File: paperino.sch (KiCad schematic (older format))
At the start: 19 parts, among them P1 CONN_01X06, P2 CONN_01X06, Q1 PMOS, Q2 NMOS, U1 BMA250E, X1 XF2M-2615-1A, X2 XF2B-4545-1A

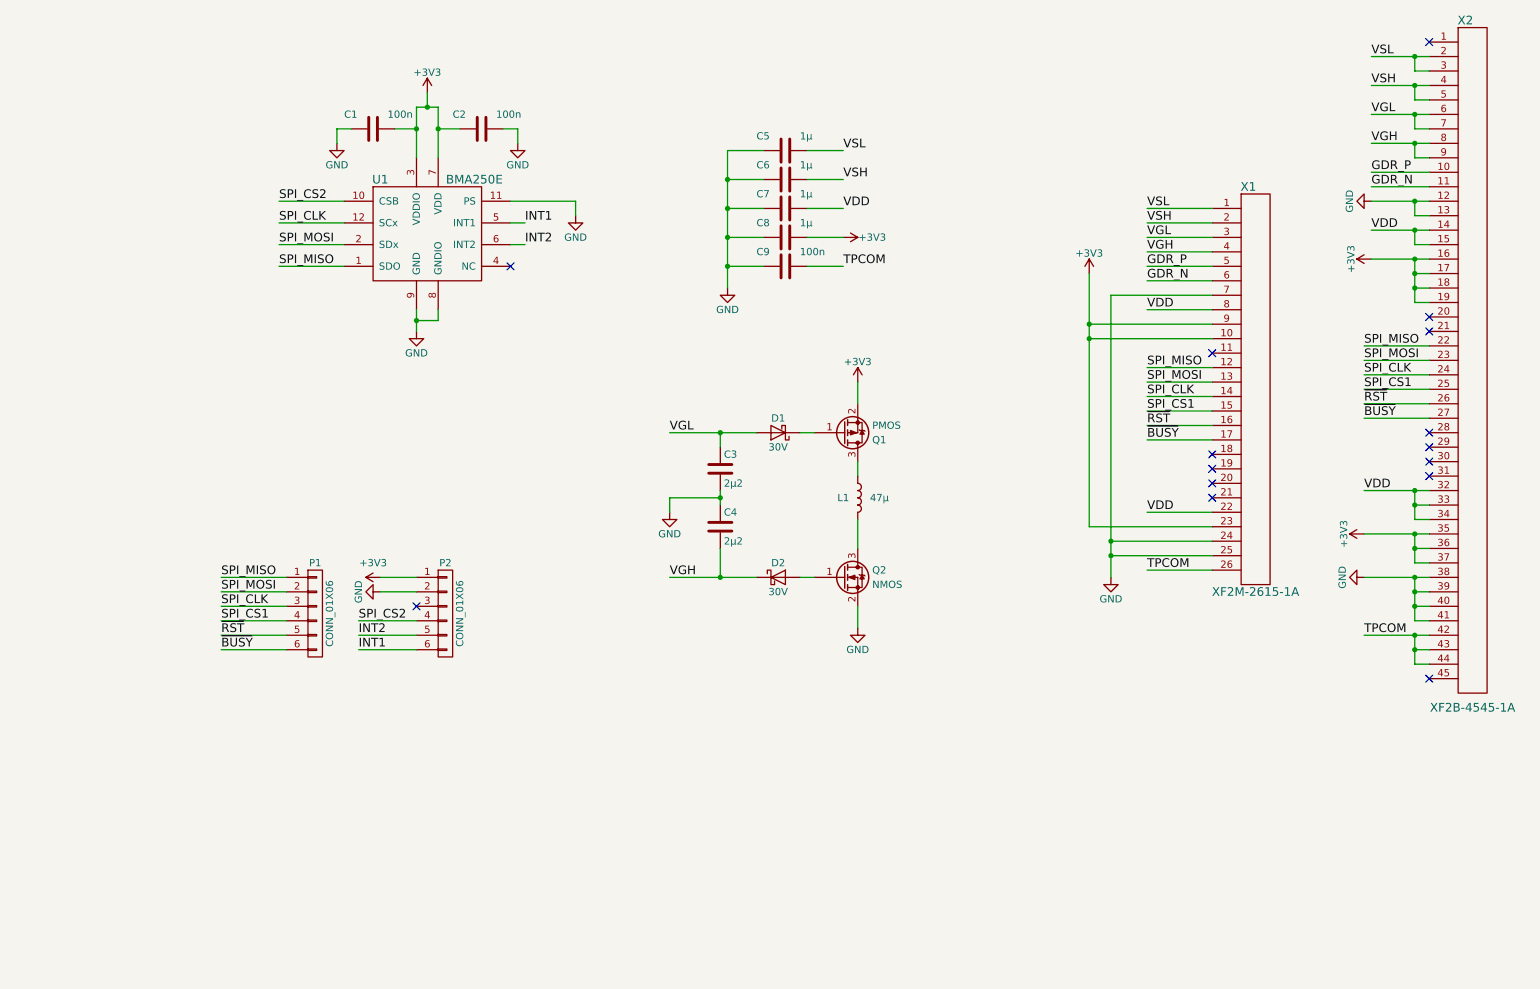
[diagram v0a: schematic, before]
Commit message: error in booster circuit corrected
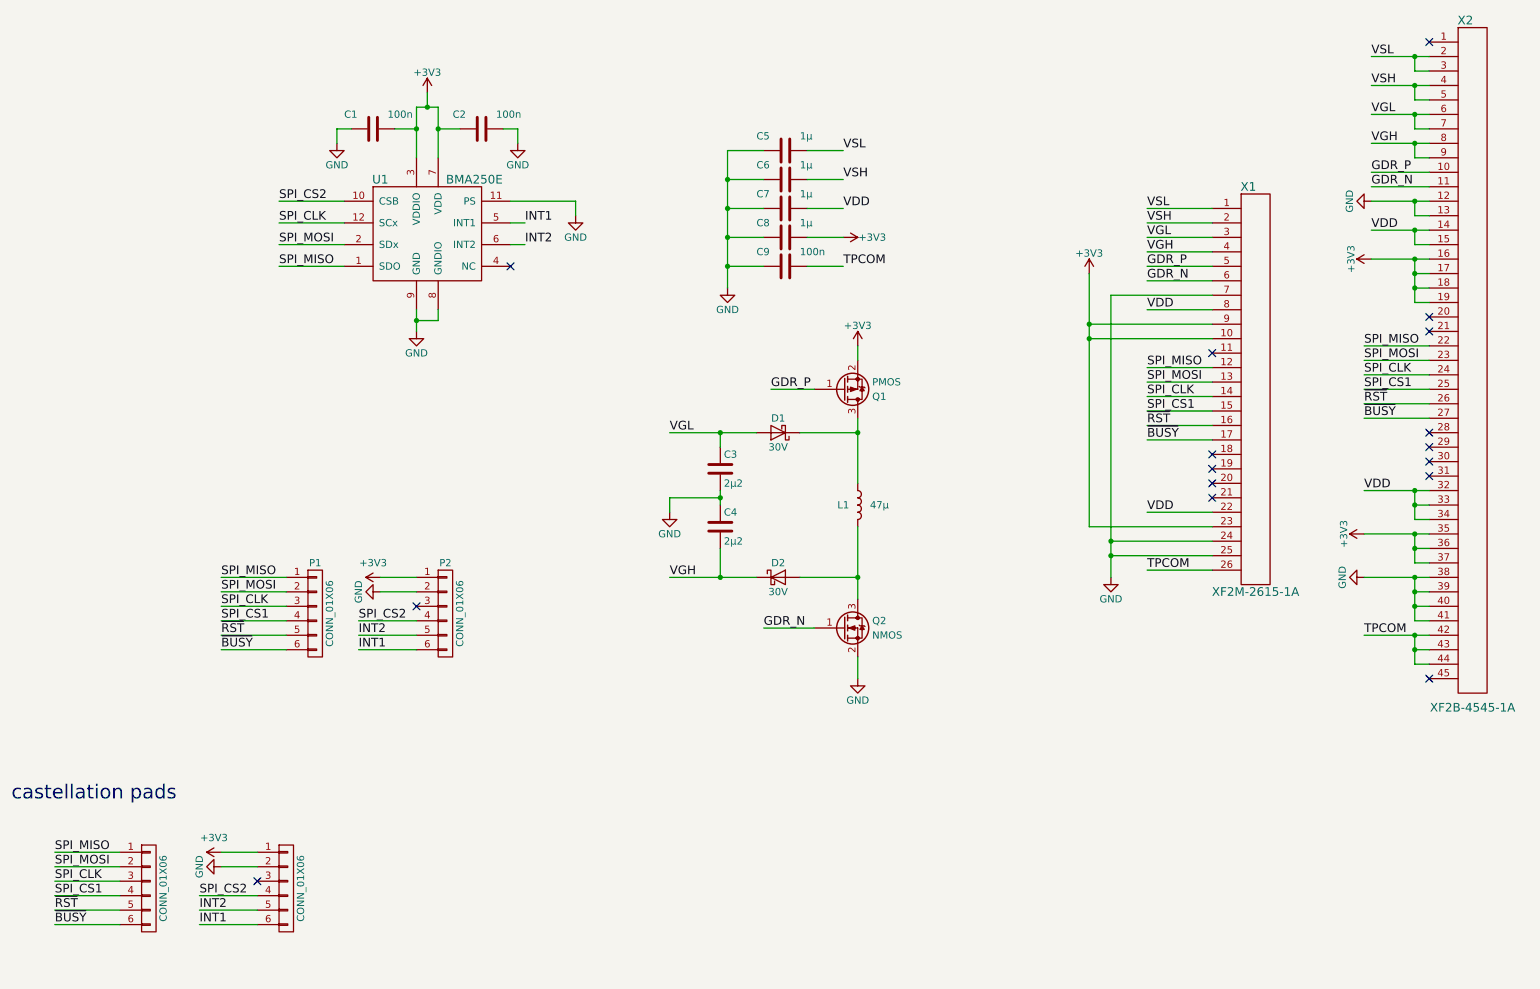
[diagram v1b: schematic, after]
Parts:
- added P3, P4: CONN_01X06, Paperino:1x6_header, symbol CONN_01X06
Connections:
- net +3V3: now also P4.1 (P1)
- net GDR_N: now also Q2.1 (G)
- net GDR_P: now also Q1.1 (G)
- net GND: now also P4.2 (P2)
- net INT1: now also P4.6 (P6)
- net INT2: now also P4.5 (P5)
- net SPI_CLK: now also P3.3 (P3)
- net SPI_CS1: now also P3.4 (P4)
- net SPI_CS2: now also P4.4 (P4)
- net SPI_MISO: now also P3.1 (P1)
- net SPI_MOSI: now also P3.2 (P2)
- net ~BUSY: now also P3.6 (P6)
- net ~RST: now also P3.5 (P5)
- net at L1.1, Q1.3 (D): now also D1.1 (K)
- net at L1.2, Q2.3 (D): now also D2.2 (A)
- no-connect marks 15 -> 16
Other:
- note added: "castellation pads"
- moved on the sheet: L1, Q1, Q2
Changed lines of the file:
@@
 L L L1
 U 1 1 589DD1F6
-P 6500 4400
-F 0 "L1" H 6400 4400 50  0000 C CNN
-F 1 "47µ" H 6650 4400 50  0000 C CNN
-F 2 "Paperino:NR4018T470M" H 6500 4400 50  0001 C CNN
-F 3 "" H 6500 4400 50  0000 C CNN
-	1    6500 4400
+P 6500 4450
+F 0 "L1" H 6400 4450 50  0000 C CNN
+F 1 "47µ" H 6650 4450 50  0000 C CNN
+F 2 "Paperino:NR4018T470M" H 6500 4450 50  0001 C CNN
+F 3 "" H 6500 4450 50  0000 C CNN
+	1    6500 4450
 	1    0    0    -1
 $EndComp
@@
 L Q_NMOS_GSD Q2
 U 1 1 589DD9DD
-P 6400 4950
-F 0 "Q2" H 6600 5000 50  0000 L CNN
-F 1 "NMOS" H 6600 4900 50  0000 L CNN
-F 2 "TO_SOT_Packages_SMD:SOT-323_SC-70" H 6600 5050 50  0001 C CNN
-F 3 "" H 6400 4950 50  0000 C CNN
-	1    6400 4950
-	1    0    0    -1
-$EndComp
-Wire Wire Line
-	6500 4750 6500 4550
+P 6400 5300
+F 0 "Q2" H 6600 5350 50  0000 L CNN
+F 1 "NMOS" H 6600 5250 50  0000 L CNN
+F 2 "TO_SOT_Packages_SMD:SOT-323_SC-70" H 6600 5400 50  0001 C CNN
+F 3 "" H 6400 5300 50  0000 C CNN
+	1    6400 5300
+	1    0    0    -1
+$EndComp
+Wire Wire Line
+	6500 4600 6500 5100
 $Comp
 L GND #PWR06
 U 1 1 589DDF8E
-P 6500 5300
-F 0 "#PWR06" H 6500 5050 50  0001 C CNN
-F 1 "GND" H 6500 5150 50  0000 C CNN
-F 2 "" H 6500 5300 50  0000 C CNN
-F 3 "" H 6500 5300 50  0000 C CNN
-	1    6500 5300
+P 6500 5650
+F 0 "#PWR06" H 6500 5400 50  0001 C CNN
+F 1 "GND" H 6500 5500 50  0000 C CNN
+F 2 "" H 6500 5650 50  0000 C CNN
+F 3 "" H 6500 5650 50  0000 C CNN
+	1    6500 5650
 	1    0    0    -1
 $EndComp
@@
 L +3V3 #PWR07
 U 1 1 589DE04D
-P 6500 3600
-F 0 "#PWR07" H 6500 3450 50  0001 C CNN
-F 1 "+3V3" H 6500 3740 50  0000 C CNN
-F 2 "" H 6500 3600 50  0000 C CNN
-F 3 "" H 6500 3600 50  0000 C CNN
-	1    6500 3600
+P 6500 3350
+F 0 "#PWR07" H 6500 3200 50  0001 C CNN
+F 1 "+3V3" H 6500 3490 50  0000 C CNN
+F 2 "" H 6500 3350 50  0000 C CNN
+F 3 "" H 6500 3350 50  0000 C CNN
+	1    6500 3350
 	1    0    0    -1
 $EndComp
@@
 L Q_PMOS_GSD Q1
 U 1 1 589DE096
-P 6400 3950
-F 0 "Q1" H 6600 4000 50  0000 L CNN
-F 1 "PMOS" H 6600 3900 50  0000 L CNN
-F 2 "Paperino:SC-59" H 6600 4050 50  0001 C CNN
-F 3 "" H 6400 3950 50  0000 C CNN
-	1    6400 3950
+P 6400 3650
+F 0 "Q1" H 6600 3700 50  0000 L CNN
+F 1 "PMOS" H 6600 3600 50  0000 L CNN
+F 2 "Paperino:SC-59" H 6600 3750 50  0001 C CNN
+F 3 "" H 6400 3650 50  0000 C CNN
+	1    6400 3650
 	1    0    0    1
 $EndComp
 Wire Wire Line
-	6500 4250 6500 4150
-Wire Wire Line
-	6500 5300 6500 5150
-Wire Wire Line
-	6500 3600 6500 3750
+	6500 5650 6500 5500
+Wire Wire Line
+	6500 3350 6500 3450
 $Comp
 L BMA250E U1
@@
 $EndComp
 Wire Wire Line
-	6100 3950 6200 3950
-Wire Wire Line
-	6100 4950 6200 4950
+	6100 3950 6500 3950
+Wire Wire Line
+	6500 4950 6100 4950
 $Comp
 L +3V3 #PWR010
@@
 Wire Wire Line
 	2100 5450 2550 5450
+$Comp
+L CONN_01X06 P3
+U 1 1 58A6EC07
+P 1600 7100
+F 0 "P3" H 1600 7450 50  0001 C CNN
+F 1 "CONN_01X06" V 1700 7100 50  0000 C CNN
+F 2 "Paperino:1x6_header" H 1600 7100 50  0001 C CNN
+F 3 "" H 1600 7100 50  0000 C CNN
+	1    1600 7100
+	1    0    0    -1
+$EndComp
+Text Label 950  6950 0    60   ~ 0
+SPI_MOSI
+Text Label 950  6850 0    60   ~ 0
+SPI_MISO
+Text Label 950  7050 0    60   ~ 0
+SPI_CLK
+Text Label 950  7150 0    60   ~ 0
+SPI_CS1
+Text Label 950  7250 0    60   ~ 0
+~RST
+Text Label 950  7350 0    60   ~ 0
+~BUSY
+Wire Wire Line
+	950  6850 1400 6850
+Wire Wire Line
+	950  6950 1400 6950
+Wire Wire Line
+	950  7050 1400 7050
+Wire Wire Line
+	950  7150 1400 7150
+Wire Wire Line
+	1400 7250 950  7250
+Wire Wire Line
+	950  7350 1400 7350
+$Comp
+L CONN_01X06 P4
+U 1 1 58A6EEF6
+P 2550 7100
+F 0 "P4" H 2550 7450 50  0001 C CNN
+F 1 "CONN_01X06" V 2650 7100 50  0000 C CNN
+F 2 "Paperino:1x6_header" H 2550 7100 50  0001 C CNN
+F 3 "" H 2550 7100 50  0000 C CNN
+	1    2550 7100
+	1    0    0    -1
+$EndComp
+Text Label 1950 7150 0    60   ~ 0
+SPI_CS2
+Text Label 1950 7250 0    60   ~ 0
+INT2
+Text Label 1950 7350 0    60   ~ 0
+INT1
+$Comp
+L +3V3 #PWR019
+U 1 1 58A6EEFF
+P 2100 6850
+F 0 "#PWR019" H 2100 6700 50  0001 C CNN
+F 1 "+3V3" V 2200 6900 50  0000 C CNN
+F 2 "" H 2100 6850 50  0000 C CNN
+F 3 "" H 2100 6850 50  0000 C CNN
+	1    2100 6850
+	0    -1   -1   0
+$EndComp
+$Comp
+L GND #PWR020
+U 1 1 58A6EF05
+P 2100 6950
+F 0 "#PWR020" H 2100 6700 50  0001 C CNN
+F 1 "GND" H 2100 6800 50  0000 C CNN
+F 2 "" H 2100 6950 50  0000 C CNN
+F 3 "" H 2100 6950 50  0000 C CNN
+	1    2100 6950
+	0    1    1    0
+$EndComp
+Wire Wire Line
+	2100 6950 2350 6950
+Wire Wire Line
+	2350 6850 2100 6850
+NoConn ~ 2350 7050
+Wire Wire Line
+	1950 7150 2350 7150
+Wire Wire Line
+	2350 7250 1950 7250
+Wire Wire Line
+	1950 7350 2350 7350
+Text Notes 650  6500 0    98   ~ 0
+castellation pads
+Text Label 5850 5300 0    60   ~ 0
+GDR_N
+Text Label 5900 3650 0    60   ~ 0
+GDR_P
+Wire Wire Line
+	5900 3650 6200 3650
+Wire Wire Line
+	5850 5300 6200 5300
+Connection ~ 6500 4950
+Wire Wire Line
+	6500 3850 6500 4300
+Connection ~ 6500 3950
 $EndSCHEMATC

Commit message: fiducials added
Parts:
- added Fid1, Fid2: Fiducial, Paperino:Fiducial, symbol Fiducial
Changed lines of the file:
@@
 U 1 1 589DD9DD
 P 6400 5300
-F 0 "Q2" H 6600 5350 50  0000 L CNN
-F 1 "NMOS" H 6600 5250 50  0000 L CNN
+F 0 "Q2" H 6600 5300 50  0000 L CNN
+F 1 "NMOS" H 6600 5250 50  0001 L CNN
 F 2 "TO_SOT_Packages_SMD:SOT-323_SC-70" H 6600 5400 50  0001 C CNN
 F 3 "" H 6400 5300 50  0000 C CNN
@@
 U 1 1 589DE096
 P 6400 3650
-F 0 "Q1" H 6600 3700 50  0000 L CNN
-F 1 "PMOS" H 6600 3600 50  0000 L CNN
+F 0 "Q1" H 6600 3650 50  0000 L CNN
+F 1 "PMOS" H 6600 3600 50  0001 L CNN
 F 2 "Paperino:SC-59" H 6600 3750 50  0001 C CNN
 F 3 "" H 6400 3650 50  0000 C CNN
@@
 P 2750 5200
 F 0 "P1" H 2750 5550 50  0000 C CNN
-F 1 "CONN_01X06" V 2850 5200 50  0000 C CNN
+F 1 "CONN_01X06" V 2850 5200 50  0001 C CNN
 F 2 "Paperino:1x6_header" H 2750 5200 50  0001 C CNN
 F 3 "" H 2750 5200 50  0000 C CNN
@@
 P 3650 5200
 F 0 "P2" H 3650 5550 50  0000 C CNN
-F 1 "CONN_01X06" V 3750 5200 50  0000 C CNN
+F 1 "CONN_01X06" V 3750 5200 50  0001 C CNN
 F 2 "Paperino:1x6_header" H 3650 5200 50  0001 C CNN
 F 3 "" H 3650 5200 50  0000 C CNN
@@
 P 1600 7100
 F 0 "P3" H 1600 7450 50  0001 C CNN
-F 1 "CONN_01X06" V 1700 7100 50  0000 C CNN
+F 1 "CONN_01X06" V 1700 7100 50  0001 C CNN
 F 2 "Paperino:1x6_header" H 1600 7100 50  0001 C CNN
 F 3 "" H 1600 7100 50  0000 C CNN
@@
 P 2550 7100
 F 0 "P4" H 2550 7450 50  0001 C CNN
-F 1 "CONN_01X06" V 2650 7100 50  0000 C CNN
+F 1 "CONN_01X06" V 2650 7100 50  0001 C CNN
 F 2 "Paperino:1x6_header" H 2550 7100 50  0001 C CNN
 F 3 "" H 2550 7100 50  0000 C CNN
@@
 	6500 3850 6500 4300
 Connection ~ 6500 3950
+$Comp
+L Fiducial Fid1
+U 1 1 58B53A2F
+P 6300 7450
+F 0 "Fid1" H 6300 7250 60  0000 C CNN
+F 1 "Fiducial" H 6300 7700 60  0001 C CNN
+F 2 "Paperino:Fiducial" H 6300 7450 60  0001 C CNN
+F 3 "" H 6300 7450 60  0001 C CNN
+	1    6300 7450
+	1    0    0    -1
+$EndComp
+$Comp
+L Fiducial Fid2
+U 1 1 58B53F28
+P 6700 7450
+F 0 "Fid2" H 6700 7250 60  0000 C CNN
+F 1 "Fiducial" H 6700 7700 60  0001 C CNN
+F 2 "Paperino:Fiducial" H 6700 7450 60  0001 C CNN
+F 3 "" H 6700 7450 60  0001 C CNN
+	1    6700 7450
+	1    0    0    -1
+$EndComp
 $EndSCHEMATC

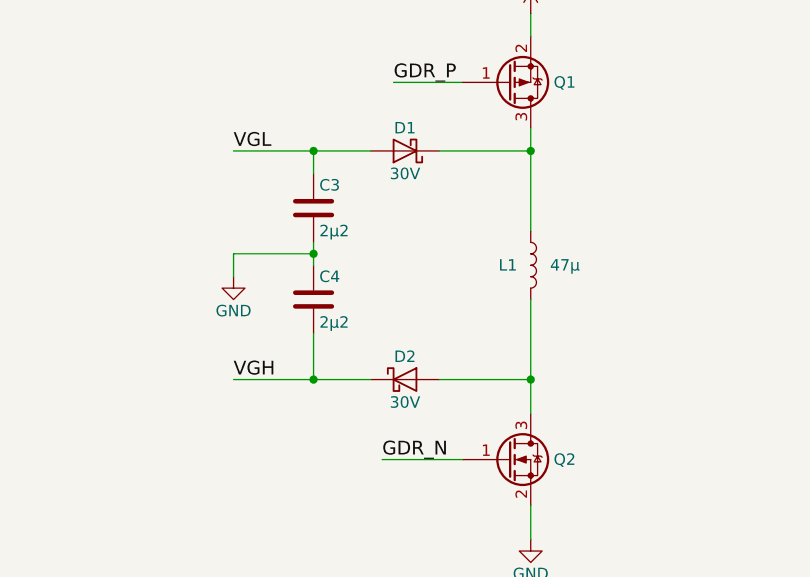
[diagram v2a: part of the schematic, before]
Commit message: component metadata
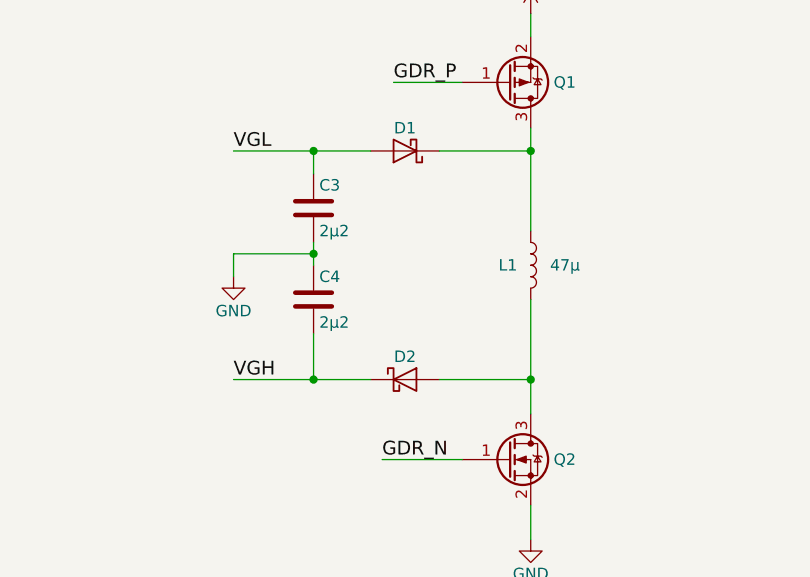
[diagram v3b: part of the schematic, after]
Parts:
- D1, D2: MFG Name (none) -> ON Semiconductor; MFG Part Num (none) -> RB751V40T1G
- Fid1, Fid2: MFG Name (none) -> N/A; MFG Part Num (none) -> N/A
- L1: MFG Name (none) -> Taiyo Yuden; MFG Part Num (none) -> NR4018T470M
- Q1: MFG Name (none) -> Infineon Technologies; MFG Part Num (none) -> BSR315PH6327XTSA1
- Q2: MFG Name (none) -> Vishay Siliconix; MFG Part Num (none) -> SI1308EDL-T1-GE3
- U1: MFG Name (none) -> Bosch Sensortec; MFG Part Num (none) -> BMA250E
- X1: MFG Name (none) -> Omron Electronics; MFG Part Num (none) -> XF2M-2615-1A
- X2: MFG Name (none) -> Omron Electronics; MFG Part Num (none) -> XF2B-4545-1A
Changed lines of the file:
@@
 F 2 "Paperino:XF2M-2615-1A" H 9150 4250 60  0001 C CNN
 F 3 "" H 9150 4250 60  0001 C CNN
+F 4 "Omron Electronics" H 9150 3650 60  0001 C CNN "MFG Name"
+F 5 "XF2M-2615-1A" H 9150 3650 60  0001 C CNN "MFG Part Num"
 	1    9150 3650
 	1    0    0    -1
@@
 F 2 "Paperino:NR4018T470M" H 6500 4450 50  0001 C CNN
 F 3 "" H 6500 4450 50  0000 C CNN
+F 4 "Taiyo Yuden" H 6500 4450 60  0001 C CNN "MFG Name"
+F 5 "NR4018T470M" H 6500 4450 60  0001 C CNN "MFG Part Num"
 	1    6500 4450
 	1    0    0    -1
@@
 F 2 "TO_SOT_Packages_SMD:SOT-323_SC-70" H 6600 5400 50  0001 C CNN
 F 3 "" H 6400 5300 50  0000 C CNN
+F 4 "Vishay Siliconix" H 6400 5300 60  0001 C CNN "MFG Name"
+F 5 "SI1308EDL-T1-GE3" H 6400 5300 60  0001 C CNN "MFG Part Num"
 	1    6400 5300
 	1    0    0    -1
@@
 F 2 "Paperino:SC-59" H 6600 3750 50  0001 C CNN
 F 3 "" H 6400 3650 50  0000 C CNN
+F 4 "Infineon Technologies" H 6400 3650 60  0001 C CNN "MFG Name"
+F 5 "BSR315PH6327XTSA1" H 6400 3650 60  0001 C CNN "MFG Part Num"
 	1    6400 3650
 	1    0    0    1
@@
 F 2 "Paperino:LGA-12-2x2x0.95" H 4600 2550 60  0001 C CNN
 F 3 "" H 4600 2550 60  0001 C CNN
+F 4 "Bosch Sensortec" H 3150 2550 60  0001 C CNN "MFG Name"
+F 5 "BMA250E" H 3150 2550 60  0001 C CNN "MFG Part Num"
 	1    3150 2550
 	1    0    0    -1
@@
 P 5950 3950
 F 0 "D1" H 5950 3850 50  0000 C CNN
-F 1 "30V" H 5950 4050 50  0000 C CNN
+F 1 "30V" H 5950 4050 50  0001 C CNN
 F 2 "Diodes_SMD:D_SOD-323" H 5950 3950 50  0001 C CNN
 F 3 "" H 5950 3950 50  0000 C CNN
+F 4 "ON Semiconductor" H 5950 3950 60  0001 C CNN "MFG Name"
+F 5 "RB751V40T1G" H 5950 3950 60  0001 C CNN "MFG Part Num"
 	1    5950 3950
 	-1   0    0    1
@@
 P 5950 4950
 F 0 "D2" H 5950 5050 50  0000 C CNN
-F 1 "30V" H 5950 4850 50  0000 C CNN
+F 1 "30V" H 5950 4850 50  0001 C CNN
 F 2 "Diodes_SMD:D_SOD-323" H 5950 4950 50  0001 C CNN
 F 3 "" H 5950 4950 50  0000 C CNN
+F 4 "ON Semiconductor" H 5950 4950 60  0001 C CNN "MFG Name"
+F 5 "RB751V40T1G" H 5950 4950 60  0001 C CNN "MFG Part Num"
 	1    5950 4950
 	1    0    0    -1
@@
 F 2 "Paperino:XF2B-4545-31A" H 10650 3100 60  0001 C CNN
 F 3 "" H 10650 3100 60  0001 C CNN
+F 4 "Omron Electronics" H 10650 2500 60  0001 C CNN "MFG Name"
+F 5 "XF2B-4545-1A" H 10650 2500 60  0001 C CNN "MFG Part Num"
 	1    10650 2500
 	1    0    0    -1
@@
 F 2 "Paperino:Fiducial" H 6300 7450 60  0001 C CNN
 F 3 "" H 6300 7450 60  0001 C CNN
+F 4 "N/A" H 6300 7450 60  0001 C CNN "MFG Name"
+F 5 "N/A" H 6300 7450 60  0001 C CNN "MFG Part Num"
 	1    6300 7450
 	1    0    0    -1
@@
 F 2 "Paperino:Fiducial" H 6700 7450 60  0001 C CNN
 F 3 "" H 6700 7450 60  0001 C CNN
+F 4 "N/A" H 6700 7450 60  0001 C CNN "MFG Name"
+F 5 "N/A" H 6700 7450 60  0001 C CNN "MFG Part Num"
 	1    6700 7450
 	1    0    0    -1
